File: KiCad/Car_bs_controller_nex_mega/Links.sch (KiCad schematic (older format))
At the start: 51 parts, among them Q1 BSS138, SW1 SW_Push, U2 ADM705, U3 MAX485E

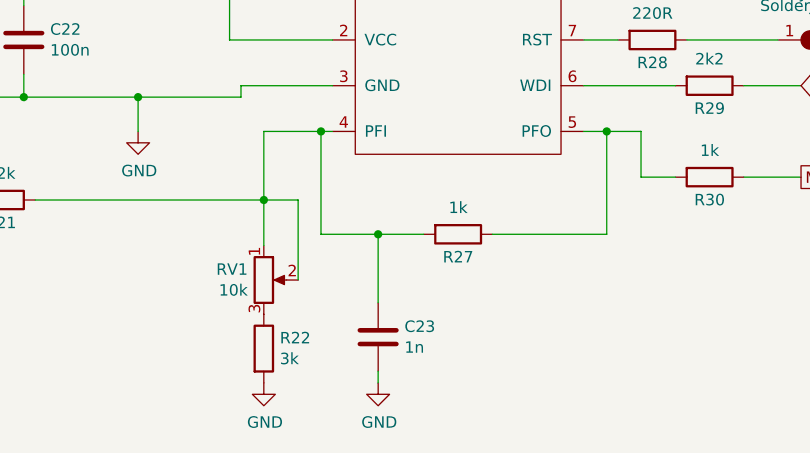
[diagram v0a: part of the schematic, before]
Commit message: wiring diagram changes
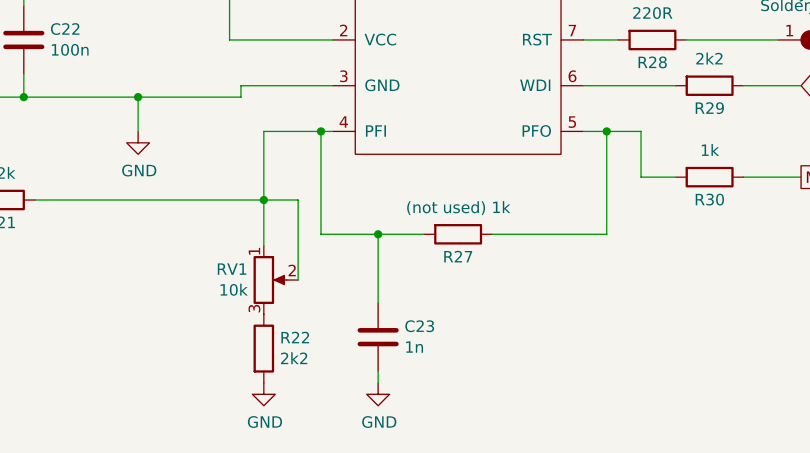
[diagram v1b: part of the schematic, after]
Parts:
- R22: value 3k -> 2k2
- R27: value 1k -> (not used) 1k
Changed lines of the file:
@@
 P 3100 7300
 F 0 "R22" H 3170 7346 50  0000 L CNN
-F 1 "3k" H 3170 7255 50  0000 L CNN
+F 1 "2k2" H 3170 7255 50  0000 L CNN
 F 2 "Resistor_SMD:R_0603_1608Metric_Pad0.98x0.95mm_HandSolder" V 3030 7300 50  0001 C CNN
 F 3 "~" H 3100 7300 50  0001 C CNN
@@
 AR Path="/5FF96CA3/608BD806" Ref="R27"  Part="1"
 F 0 "R27" V 4050 6800 50  0000 C CNN
-F 1 "1k" V 3834 6800 50  0000 C CNN
+F 1 "(not used) 1k" V 3834 6800 50  0000 C CNN
 F 2 "Resistor_SMD:R_0603_1608Metric_Pad0.98x0.95mm_HandSolder" V 3880 6800 50  0001 C CNN
 F 3 "~" H 3950 6800 50  0001 C CNN

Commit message: Changes
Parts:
- R32: value 1k2 -> 2k2
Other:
- note added: "Optional"
- moved on the sheet: D32, R32
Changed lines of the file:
@@
 L Car_bs_controller_nex_mega-rescue:LED-Device D32
 U 1 1 601BAB6B
-P 6750 4850
-F 0 "D32" V 6789 4930 50  0000 L CNN
-F 1 "LED_PJ" V 6698 4930 50  0000 L CNN
-F 2 "LED_SMD:LED_0603_1608Metric" H 6750 4850 50  0001 C CNN
-F 3 "~" H 6750 4850 50  0001 C CNN
-	1    6750 4850
+P 6750 4350
+F 0 "D32" V 6789 4430 50  0000 L CNN
+F 1 "LED_PJ" V 6698 4430 50  0000 L CNN
+F 2 "LED_SMD:LED_0603_1608Metric" H 6750 4350 50  0001 C CNN
+F 3 "~" H 6750 4350 50  0001 C CNN
+	1    6750 4350
 	0    1    -1   0
 $EndComp
@@
 L Car_bs_controller_nex_mega-rescue:R-Device R32
 U 1 1 601BAB71
-P 6750 4500
-F 0 "R32" H 6820 4546 50  0000 L CNN
-F 1 "1k2" H 6820 4455 50  0000 L CNN
-F 2 "Resistor_SMD:R_0603_1608Metric" V 6680 4500 50  0001 C CNN
-F 3 "~" H 6750 4500 50  0001 C CNN
-	1    6750 4500
-	1    0    0    -1
-$EndComp
-Wire Wire Line
-	6750 4350 6750 4300
-Wire Wire Line
-	6750 4700 6750 4650
+P 6750 4000
+F 0 "R32" H 6820 4046 50  0000 L CNN
+F 1 "2k2" H 6820 3955 50  0000 L CNN
+F 2 "Resistor_SMD:R_0603_1608Metric" V 6680 4000 50  0001 C CNN
+F 3 "~" H 6750 4000 50  0001 C CNN
+	1    6750 4000
+	1    0    0    -1
+$EndComp
+Wire Wire Line
+	6750 3850 6750 3800
+Wire Wire Line
+	6750 4200 6750 4150
 $Comp
 L Car_bs_controller_nex_mega-rescue:GND-power #PWR044
 U 1 1 601BAB79
-P 6750 5100
-F 0 "#PWR044" H 6750 4850 50  0001 C CNN
-F 1 "GND" H 6755 4927 50  0000 C CNN
-F 2 "" H 6750 5100 50  0001 C CNN
-F 3 "" H 6750 5100 50  0001 C CNN
-	1    6750 5100
-	1    0    0    -1
-$EndComp
-Wire Wire Line
-	6750 5100 6750 5000
-Text GLabel 6500 4300 0    50   Input ~ 0
+P 6750 4600
+F 0 "#PWR044" H 6750 4350 50  0001 C CNN
+F 1 "GND" H 6755 4427 50  0000 C CNN
+F 2 "" H 6750 4600 50  0001 C CNN
+F 3 "" H 6750 4600 50  0001 C CNN
+	1    6750 4600
+	1    0    0    -1
+$EndComp
+Wire Wire Line
+	6750 4600 6750 4500
+Text GLabel 6500 3800 0    50   Input ~ 0
 MCU_system_status_LED
 Wire Wire Line
-	6500 4300 6750 4300
+	6500 3800 6750 3800
 Connection ~ 3000 1500
 Connection ~ 3400 3050
@@
 Wire Wire Line
 	2050 5650 2950 5650
+Wire Notes Line
+	6700 4900 6700 7700
+Wire Notes Line
+	6700 7700 600  7700
+Wire Notes Line
+	600  7700 600  4900
+Wire Notes Line
+	600  4900 6700 4900
+Text Notes 1150 7350 0    79   ~ 16
+Optional
 $EndSCHEMATC
